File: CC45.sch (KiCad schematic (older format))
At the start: 21 parts, among them J1 AVR-ISP-6, SW1 RESET, U1 ATmega32U4-AU, U2 PRTR5V0U2X, X1 XTAL

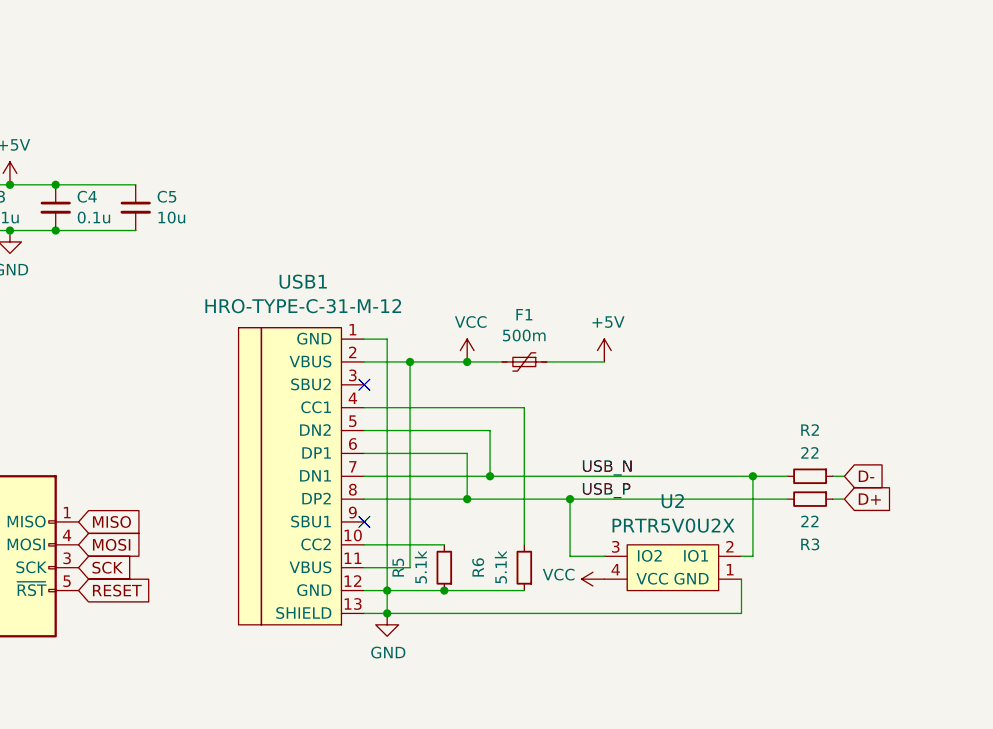
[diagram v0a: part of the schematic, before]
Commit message: Remove usb port and safeties, add jst connector
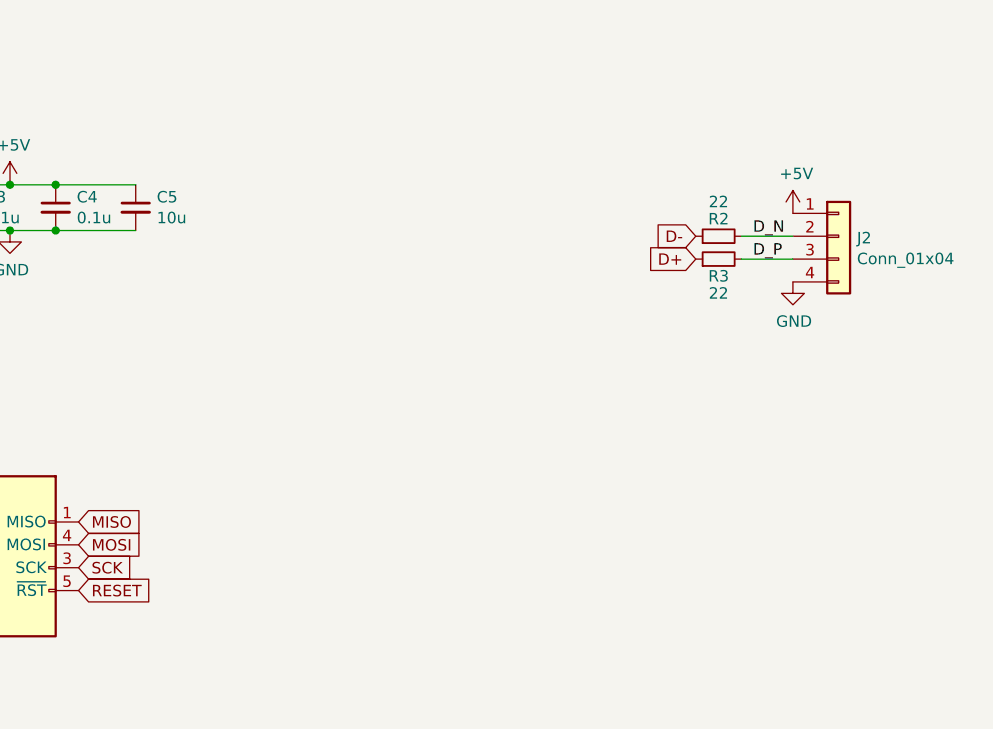
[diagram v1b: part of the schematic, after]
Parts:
- removed F1: 500m, Fuse:Fuse_1206_3216Metric_Pad1.42x1.75mm_HandSolder, symbol Device:Polyfuse_Small
- removed R5, R6: 5.1k, Resistor_SMD:R_1206_3216Metric_Pad1.42x1.75mm_HandSolder, symbol Device:R_Small
- removed U2: PRTR5V0U2X, random-keyboard-parts:SOT143B, symbol random-keyboard-parts:PRTR5V0U2X
- removed USB1: HRO-TYPE-C-31-M-12, Type-C:HRO-TYPE-C-31-M-12-HandSoldering, symbol Type-C:HRO-TYPE-C-31-M-12
- added J2: Conn_01x04, random-keyboard-parts:JST-SR-4, symbol Connector_Generic:Conn_01x04
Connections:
- net +5V: now also J2.1 (Pin_1)
- net GND: now also J2.4 (Pin_4)
- net USB_N renamed D_N
- net D_N: now also J2.2 (Pin_2)
- net USB_P renamed D_P
- net D_P: now also J2.3 (Pin_3)
- no-connect marks 8 -> 6
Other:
- moved on the sheet: R2, R3
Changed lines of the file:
@@
 	1600 7100 1700 7100
-$Comp
-L Type-C:HRO-TYPE-C-31-M-12 USB1
-U 1 1 5EF1F24B
-P 4350 6450
-F 0 "USB1" H 4183 7249 60  0000 C CNN
-F 1 "HRO-TYPE-C-31-M-12" H 4183 7142 60  0000 C CNN
-F 2 "Type-C:HRO-TYPE-C-31-M-12-HandSoldering" H 4350 6450 60  0001 C CNN
-F 3 "" H 4350 6450 60  0001 C CNN
-	1    4350 6450
-	1    0    0    -1
-$EndComp
-Wire Wire Line
-	4450 6400 4900 6400
-Wire Wire Line
-	4450 6300 5000 6300
-Wire Wire Line
-	4450 5900 4550 5900
-Wire Wire Line
-	4550 5900 4550 7000
-Wire Wire Line
-	4550 7100 4450 7100
-Wire Wire Line
-	4450 7000 4550 7000
-Connection ~ 4550 7000
-Wire Wire Line
-	4550 7000 4550 7100
-Wire Wire Line
-	4450 6000 4650 6000
-Wire Wire Line
-	4650 6000 4650 6900
-Wire Wire Line
-	4650 6900 4450 6900
-$Comp
-L power:VCC #PWR0113
-U 1 1 5EF3971F
-P 4900 6000
-F 0 "#PWR0113" H 4900 5850 50  0001 C CNN
-F 1 "VCC" H 4917 6173 50  0000 C CNN
-F 2 "" H 4900 6000 50  0001 C CNN
-F 3 "" H 4900 6000 50  0001 C CNN
-	1    4900 6000
-	1    0    0    -1
-$EndComp
-Wire Wire Line
-	4900 6000 4650 6000
-Connection ~ 4650 6000
-$Comp
-L Device:Polyfuse_Small F1
-U 1 1 5EF3A4C3
-P 5150 6000
-F 0 "F1" V 4945 6000 50  0000 C CNN
-F 1 "500m" V 5036 6000 50  0000 C CNN
-F 2 "Fuse:Fuse_1206_3216Metric_Pad1.42x1.75mm_HandSolder" H 5200 5800 50  0001 L CNN
-F 3 "~" H 5150 6000 50  0001 C CNN
-F 4 "C151162" H 5150 6000 50  0001 C CNN "LCSC"
-	1    5150 6000
-	0    1    1    0
-$EndComp
 $Comp
 L power:+5V #PWR0114
 U 1 1 5EF3A9BC
-P 5500 6000
-F 0 "#PWR0114" H 5500 5850 50  0001 C CNN
-F 1 "+5V" H 5515 6173 50  0000 C CNN
-F 2 "" H 5500 6000 50  0001 C CNN
-F 3 "" H 5500 6000 50  0001 C CNN
-	1    5500 6000
-	1    0    0    -1
-$EndComp
-Wire Wire Line
-	4900 6000 5050 6000
-Connection ~ 4900 6000
-Wire Wire Line
-	5250 6000 5500 6000
-NoConn ~ 4450 6700
-NoConn ~ 4450 6100
-$Comp
-L Device:R_Small R5
-U 1 1 5F0D60A8
-P 4800 6900
-F 0 "R5" V 5000 6900 50  0000 C CNN
-F 1 "5.1k" V 4900 6900 50  0000 C CNN
-F 2 "Resistor_SMD:R_1206_3216Metric_Pad1.42x1.75mm_HandSolder" H 4800 6900 50  0001 C CNN
-F 3 "~" H 4800 6900 50  0001 C CNN
-F 4 "C26033" H 4800 6900 50  0001 C CNN "LCSC"
-	1    4800 6900
-	-1   0    0    1
-$EndComp
-$Comp
-L Device:R_Small R6
-U 1 1 5EF3D1E8
-P 5150 6900
-F 0 "R6" V 5350 6900 50  0000 C CNN
-F 1 "5.1k" V 5250 6900 50  0000 C CNN
-F 2 "Resistor_SMD:R_1206_3216Metric_Pad1.42x1.75mm_HandSolder" H 5150 6900 50  0001 C CNN
-F 3 "~" H 5150 6900 50  0001 C CNN
-F 4 "C26033" H 5150 6900 50  0001 C CNN "LCSC"
-	1    5150 6900
-	-1   0    0    1
-$EndComp
-$Comp
-L power:GND #PWR0115
-U 1 1 5EF44303
-P 4550 7100
-F 0 "#PWR0115" H 4550 6850 50  0001 C CNN
-F 1 "GND" H 4555 6927 50  0000 C CNN
-F 2 "" H 4550 7100 50  0001 C CNN
-F 3 "" H 4550 7100 50  0001 C CNN
-	1    4550 7100
-	1    0    0    -1
-$EndComp
-Wire Wire Line
-	4550 7000 4800 7000
-Connection ~ 4800 7000
-Wire Wire Line
-	4800 7000 5150 7000
-Wire Wire Line
-	4800 6800 4450 6800
-Wire Wire Line
-	5150 6800 5150 6200
-Wire Wire Line
-	5150 6200 4450 6200
+P 6325 5350
+F 0 "#PWR0114" H 6325 5200 50  0001 C CNN
+F 1 "+5V" H 6340 5523 50  0000 C CNN
+F 2 "" H 6325 5350 50  0001 C CNN
+F 3 "" H 6325 5350 50  0001 C CNN
+	1    6325 5350
+	1    0    0    -1
+$EndComp
 $Comp
 L Device:R_Small R3
 U 1 1 5F0D60A7
-P 6400 6600
-F 0 "R3" V 6600 6600 50  0000 C CNN
-F 1 "22" V 6500 6600 50  0000 C CNN
-F 2 "Resistor_SMD:R_1206_3216Metric_Pad1.42x1.75mm_HandSolder" H 6400 6600 50  0001 C CNN
-F 3 "~" H 6400 6600 50  0001 C CNN
-F 4 "C17958" H 6400 6600 50  0001 C CNN "LCSC"
-	1    6400 6600
-	0    1    1    0
-$EndComp
-Connection ~ 5000 6500
-Wire Wire Line
-	4450 6600 4900 6600
-Wire Wire Line
-	4450 6500 5000 6500
-Wire Wire Line
-	5000 6300 5000 6500
-Wire Wire Line
-	4900 6400 4900 6600
-Connection ~ 4900 6600
-Wire Wire Line
-	6500 6600 6550 6600
-Text GLabel 6550 6500 2    50   Input ~ 0
+P 6000 5550
+F 0 "R3" V 5925 5550 50  0000 C CNN
+F 1 "22" V 5850 5550 50  0000 C CNN
+F 2 "Resistor_SMD:R_1206_3216Metric_Pad1.42x1.75mm_HandSolder" H 6000 5550 50  0001 C CNN
+F 3 "~" H 6000 5550 50  0001 C CNN
+F 4 "C17958" H 6000 5550 50  0001 C CNN "LCSC"
+	1    6000 5550
+	0    -1   -1   0
+$EndComp
+Text GLabel 5900 5450 0    50   Input ~ 0
 D-
-Text GLabel 6550 6600 2    50   Input ~ 0
+Text GLabel 5900 5550 0    50   Input ~ 0
 D+
-Wire Wire Line
-	6500 6500 6550 6500
 $Comp
 L Device:R_Small R2
 U 1 1 5EF21070
-P 6400 6500
-F 0 "R2" V 6200 6500 50  0000 C CNN
-F 1 "22" V 6300 6500 50  0000 C CNN
-F 2 "Resistor_SMD:R_1206_3216Metric_Pad1.42x1.75mm_HandSolder" H 6400 6500 50  0001 C CNN
-F 3 "~" H 6400 6500 50  0001 C CNN
-F 4 "C17958" H 6400 6500 50  0001 C CNN "LCSC"
-	1    6400 6500
-	0    1    1    0
-$EndComp
-Connection ~ 4550 7100
-$Comp
-L power:VCC #PWR0116
-U 1 1 5EF4F905
-P 5500 6950
-F 0 "#PWR0116" H 5500 6800 50  0001 C CNN
-F 1 "VCC" V 5518 7077 50  0000 L CNN
-F 2 "" H 5500 6950 50  0001 C CNN
-F 3 "" H 5500 6950 50  0001 C CNN
-	1    5500 6950
+P 6000 5450
+F 0 "R2" V 6075 5450 50  0000 C CNN
+F 1 "22" V 6150 5450 50  0000 C CNN
+F 2 "Resistor_SMD:R_1206_3216Metric_Pad1.42x1.75mm_HandSolder" H 6000 5450 50  0001 C CNN
+F 3 "~" H 6000 5450 50  0001 C CNN
+F 4 "C17958" H 6000 5450 50  0001 C CNN "LCSC"
+	1    6000 5450
 	0    -1   -1   0
 $EndComp
-$Comp
-L random-keyboard-parts:PRTR5V0U2X U2
-U 1 1 5EF49C6E
-P 5800 6900
-F 0 "U2" H 5800 6611 60  0000 C CNN
-F 1 "PRTR5V0U2X" H 5800 6718 60  0000 C CNN
-F 2 "random-keyboard-parts:SOT143B" H 5800 6900 60  0001 C CNN
-F 3 "" H 5800 6900 60  0001 C CNN
-F 4 "C78442" H 5800 6900 50  0001 C CNN "LCSC"
-	1    5800 6900
-	-1   0    0    1
-$EndComp
-Wire Wire Line
-	5500 6850 5350 6850
-Wire Wire Line
-	6100 7100 4550 7100
-Wire Wire Line
-	6100 6850 6150 6850
-Wire Wire Line
-	6100 6950 6100 7100
 Wire Wire Line
 	1700 5750 1700 5850
@@
 	1    0    0    -1
 $EndComp
-Text Label 5400 6500 0    50   ~ 0
-USB_N
-Text Label 5400 6600 0    50   ~ 0
-USB_P
-Wire Wire Line
-	5350 6850 5350 6600
-Connection ~ 5350 6600
-Wire Wire Line
-	5350 6600 6300 6600
-Wire Wire Line
-	4900 6600 5350 6600
-Wire Wire Line
-	6150 6850 6150 6500
-Connection ~ 6150 6500
-Wire Wire Line
-	6150 6500 6300 6500
-Wire Wire Line
-	5000 6500 6150 6500
 Connection ~ 2350 5425
 Wire Wire Line
@@
 NoConn ~ 2550 2950
 NoConn ~ 2550 1450
+Wire Wire Line
+	6100 5450 6325 5450
+Wire Wire Line
+	6100 5550 6325 5550
+Text Label 6150 5450 0    50   ~ 0
+D_N
+Text Label 6150 5550 0    50   ~ 0
+D_P
+$Comp
+L power:GND #PWR0115
+U 1 1 5EF44303
+P 6325 5650
+F 0 "#PWR0115" H 6325 5400 50  0001 C CNN
+F 1 "GND" H 6330 5477 50  0000 C CNN
+F 2 "" H 6325 5650 50  0001 C CNN
+F 3 "" H 6325 5650 50  0001 C CNN
+	1    6325 5650
+	1    0    0    -1
+$EndComp
+$Comp
+L Connector_Generic:Conn_01x04 J2
+U 1 1 6136D405
+P 6525 5450
+F 0 "J2" H 6605 5442 50  0000 L CNN
+F 1 "Conn_01x04" H 6605 5351 50  0000 L CNN
+F 2 "random-keyboard-parts:JST-SR-4" H 6525 5450 50  0001 C CNN
+F 3 "~" H 6525 5450 50  0001 C CNN
+	1    6525 5450
+	1    0    0    -1
+$EndComp
 $EndSCHEMATC
